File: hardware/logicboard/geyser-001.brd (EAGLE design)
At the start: 47 x 47 mm, 13 parts, among them T1 2SC1815

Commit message: New layout.
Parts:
- C1: value (none) -> 104
- D1: value 1N4004 -> 200mA/100V/1V; device diode:DO41-10 -> SparkFun-DiscreteSemi:DIODE-1N4148
- VIN, VOUT: device SparkFun-Connectors:1X02_LOCK -> SparkFun-Connectors:JST-2-PTH-NS
- moved VIN 35.9 mm to (41.0, 10.0), turned to 270 degrees
- moved T1 18.0 mm to (20.3, 6.35), turned to 0 degrees
- moved R1 17.1 mm to (15.2, 7.62)
- moved R2 16.6 mm to (41.9, 20.3)
- moved RELAY 11.7 mm to (7.62, 17.8), turned to 0 degrees
- moved LED 10.5 mm to (41.9, 16.5)
- moved VOUT 7.63 mm to (6.00, 10.0)
- moved ON-INT 7.62 mm to (21.6, 16.5)
- moved VOLTAGE-SELECT 7.62 mm to (30.5, 6.35)
- moved OFF-INT 7.62 mm to (33.0, 16.5)
- moved C1 4.58 mm to (11.4, 10.2)
- moved D1 2.54 mm to (15.2, 16.5)
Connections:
- removed net N$1: RELAY.5, VOUT.1
- new net VOUT: RELAY.5, VOUT.2
- net GND: now also VIN.1, VOUT.1; no longer VIN.2, VOUT.2
- net VDD: now also VIN.2; no longer VIN.1
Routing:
- net N$9: track 90.4 -> 46.6 mm
- net N$10: track 48.7 -> 84.8 mm, vias 0 -> 1
- net GND: track 54.5 -> 84.5 mm, vias 0 -> 1
- net VDD: track 32.9 -> 61.0 mm
- net N$8: track 69.9 -> 93.4 mm, vias 2 -> 1
- net VCC: track 59.0 -> 81.5 mm
- net RELAYDRIVE: track 2.60 -> 20.5 mm
- net LEDDRIVE: track 48.8 -> 31.4 mm
- net N$6: track 45.8 -> 57.6 mm, vias 1 -> 0
- net VOUT: track 0.00 -> 8.46 mm
- net N$5: track 49.4 -> 56.9 mm, vias 1 -> 0
- net N$11: track 42.1 -> 48.7 mm, vias 0 -> 1
- net N$1: track 5.57 -> 0.00 mm
- net N$4: track 16.6 -> 21.8 mm
- net VIN: track 26.4 -> 22.0 mm
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- added copper zone on layer 1, net N$1
- added copper zone on layer 16, net N$12
- removed copper zone on layer 1, net N$12
- removed copper zone on layer 16, net N$13

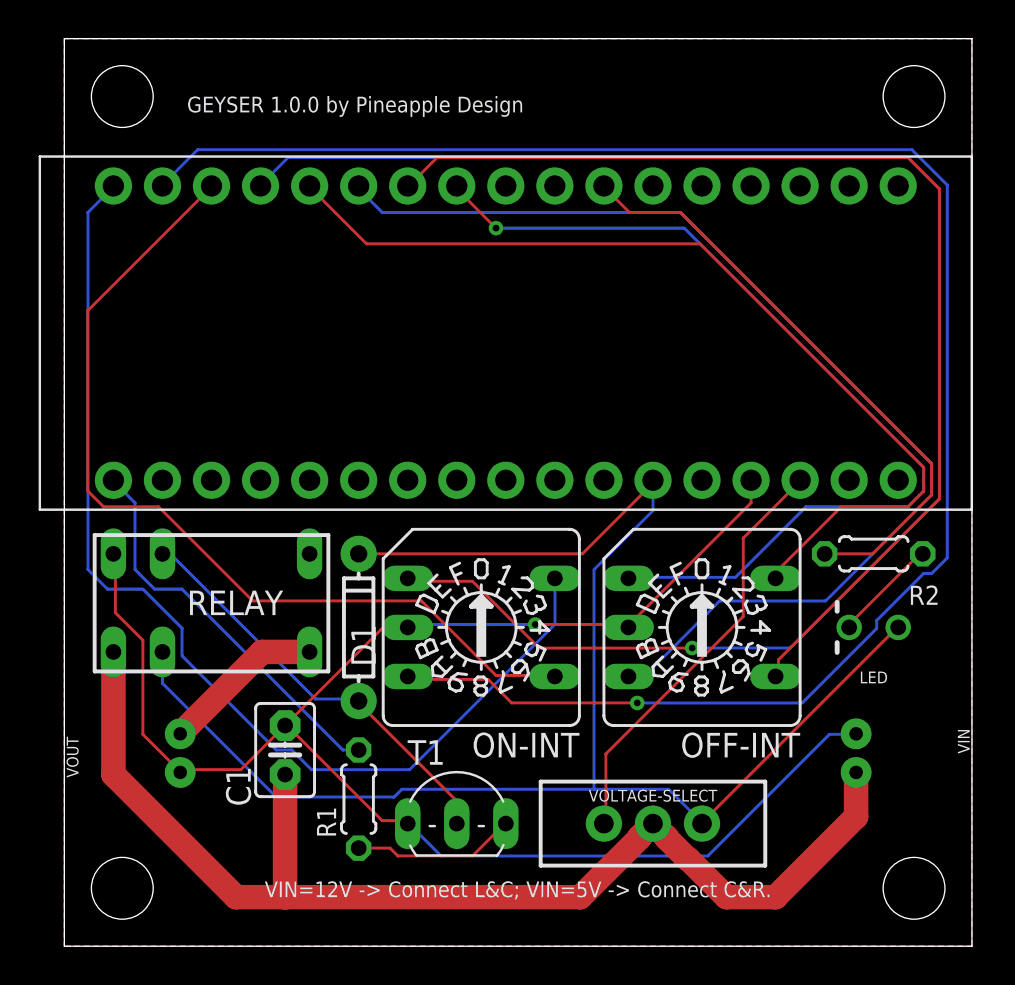
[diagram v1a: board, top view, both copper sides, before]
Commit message: Swapped + and -. Now + is on No.1 pin.
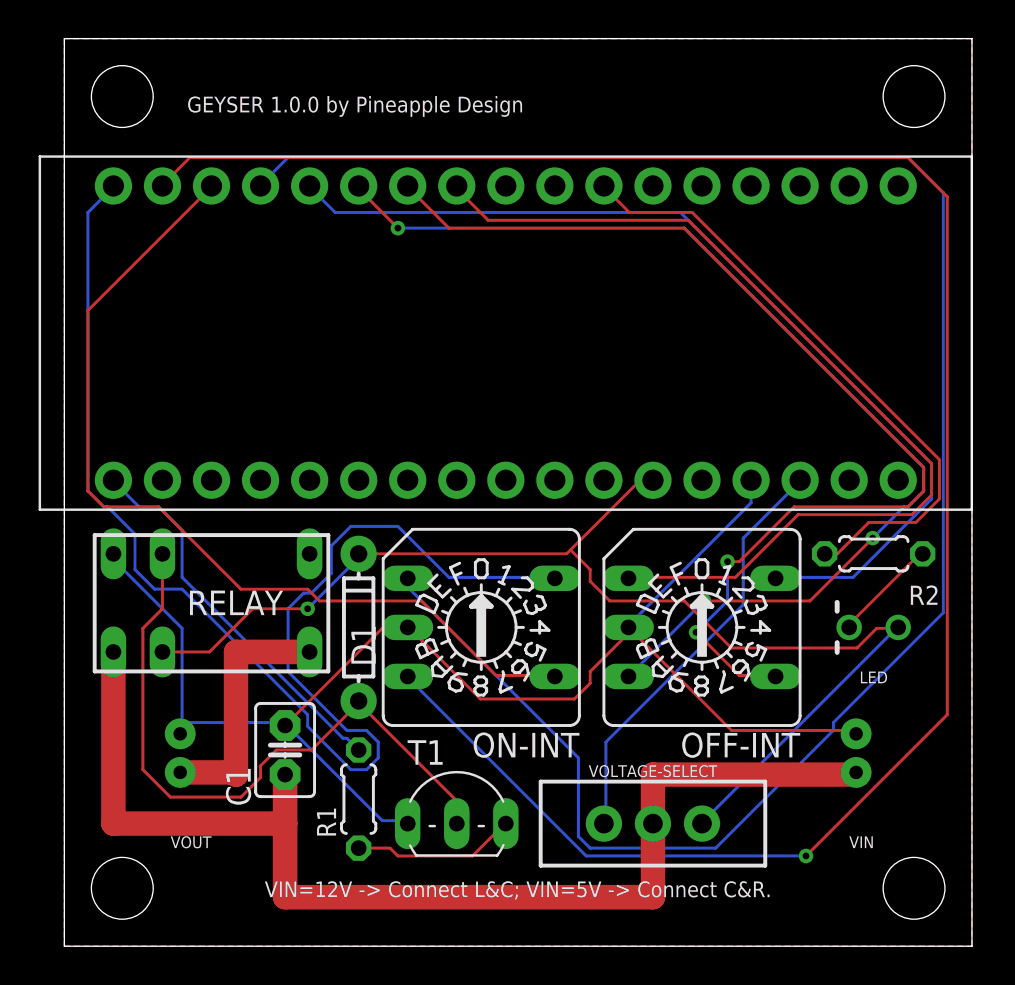
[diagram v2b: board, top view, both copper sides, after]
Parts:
- R2: value 220 -> 330
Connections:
- net GND: now also VOUT.2; no longer VOUT.1
- net VOUT: now also VOUT.1; no longer VOUT.2
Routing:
- net VCC: track 81.5 -> 63.5 mm, vias 0 -> 1
- net N$10: track 84.8 -> 99.9 mm, vias 1 -> 0
- net N$4: track 21.8 -> 34.2 mm
- net N$7: track 55.2 -> 66.8 mm
- net GND: track 84.5 -> 73.2 mm, vias 1 -> 0
- net N$8: track 93.4 -> 103.8 mm
- net VOUT: track 8.46 -> 13.1 mm
- net N$6: track 57.6 -> 55.1 mm, vias 0 -> 2
- net N$5: track 56.9 -> 55.9 mm, vias 0 -> 3
- net N$11: track 48.7 -> 49.7 mm, vias 1 -> 0
- net LEDDRIVE: track 31.4 -> 32.4 mm
- net N$2: track 48.8 -> 49.8 mm
- net VDD: track 61.0 -> 60.1 mm
- net RELAYDRIVE: track 20.5 -> 19.9 mm
- added copper zone on layer 1, net GND
- added copper zone on layer 16, net GND
- removed copper zone on layer 1, net N$1
- removed copper zone on layer 16, net N$12
